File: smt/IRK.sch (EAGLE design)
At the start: 40 parts, among them IC1 PIC18F25K50, Q1 MMBT2222A, Q2 2N7002, Q3 2N7002, Q4 TSOP4838, Q5 MMBT3906

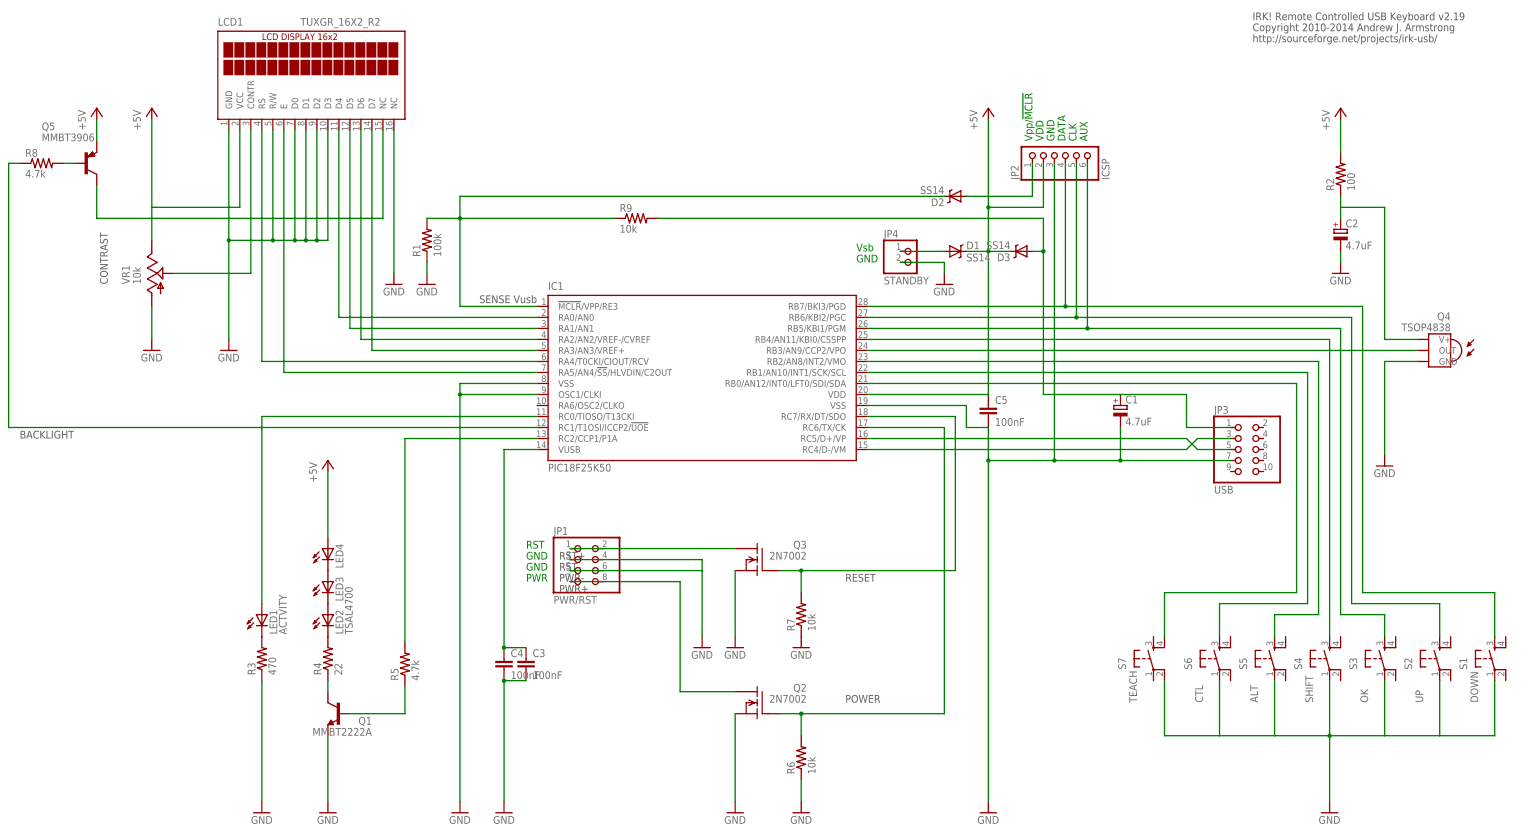
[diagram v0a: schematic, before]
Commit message: Reworked project structure to accommodate SMD and THT versions.
The orginal Through Hole Technology (THT) version is now stored
in the tht/ directory and the new Surface Mount Technology (SMT)
version is stored in the smt/ directory.
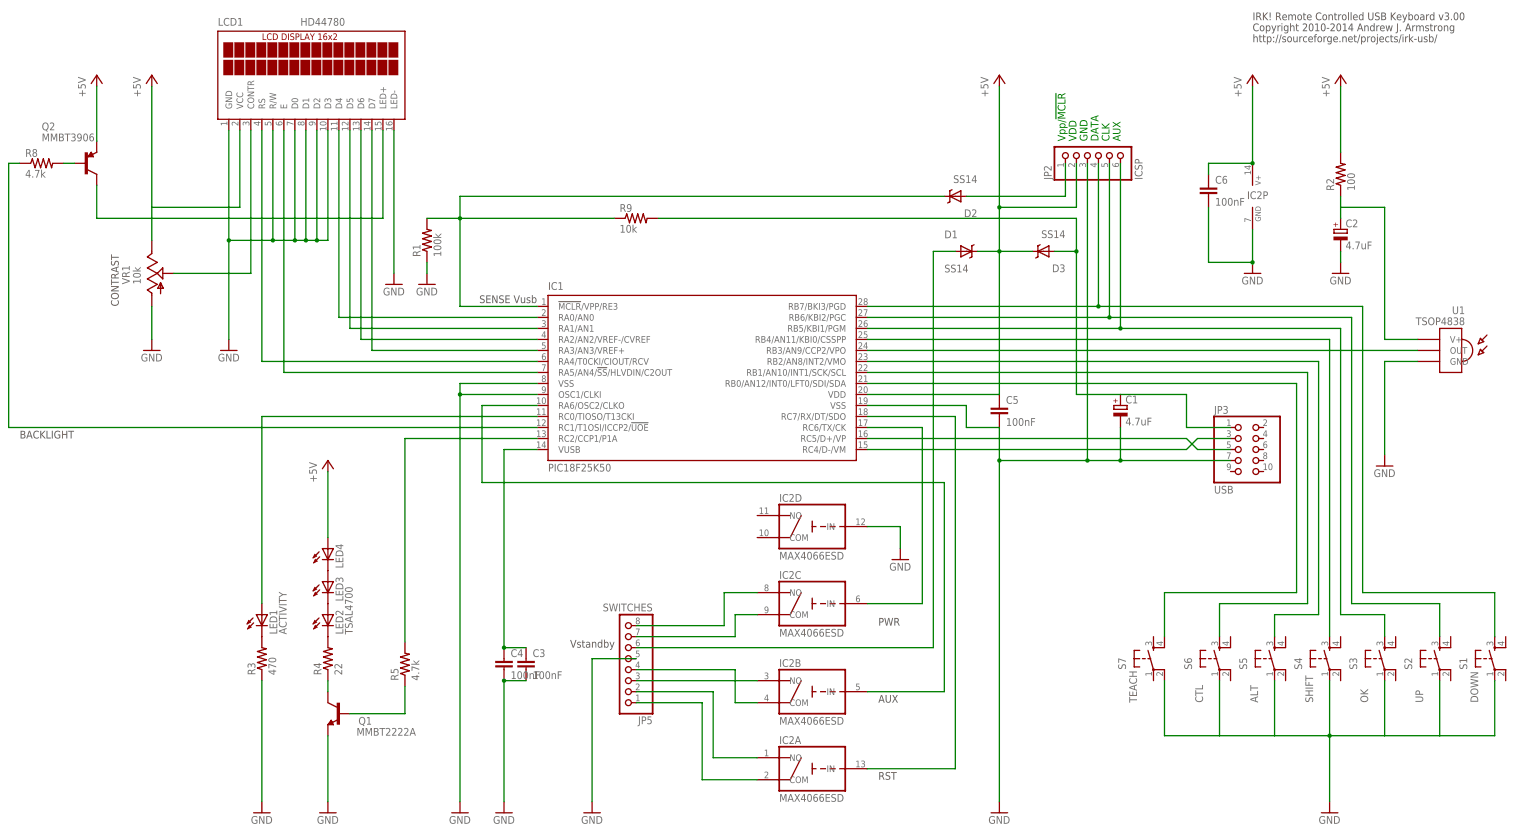
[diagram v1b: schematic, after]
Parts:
- removed JP1: PWR/RST, pinhead:PINHD-2X4
- removed JP4: STANDBY, pinhead:PINHD-1X2
- removed Q3: 2N7002, transistors_gaui:2N7002
- removed Q4: TSOP4838, tsop:TSOP4838
- removed Q5: MMBT3906, transistor-pnp:MMBT3906LT1SMD
- removed R6, R7: 10k, rcl:R-US_M1206
- added C6: 100nF, rcl:C-EUC0805
- added IC2: MAX4066ESD, irk:MAX4066ESD
- added JP5: SWITCHES, pinhead:PINHD-1X8
- added U1: TSOP4838, irk:TSOP4838
- D1, D2, D3: device SparkFun-DiscreteSemi:DIODE-SCHOTTKY_ -> irk:SS14
- LCD1: value TUXGR_16X2_R2 -> HD44780; device offboard:TUXGR_16X2_R2 -> irk:HD44780
- LED1: value ACTVITY -> ACTIVITY
- LED3, LED4: value (none) -> (none)
- Q1: device transistor:BC846A-NPN-SOT23-BEC -> irk:MMBT2222A
- Q2: value 2N7002 -> MMBT3906; device transistors_gaui:2N7002 -> irk:MMBT3906SOT23
- S1, S2, S3, S4, S5, S6, S7: device SparkFun-Electromechanical:TAC_SWITCHSMD -> irk:TAC_SWITCHPTH525
- VR1: device pot:TRIM_US-3223W -> irk:TRIMPOT3303W
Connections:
- removed net N$32: D1.A, JP4.1
- removed net N$37: IC1.RC6/TX/CK, Q2.G, R6.2
- removed net N$9: IC1.RC7/RX/DT/SDO, Q3.G, R7.2
- new net AUX: IC1.RA6/OSC2/CLKO, IC2B.IN
- new net N$33: IC2B.COM, JP5.4
- new net N$35: IC2B.NO, JP5.3
- new net N$39: IC2C.COM, JP5.7
- new net N$40: IC2C.NO, JP5.8
- new net PWR: IC1.RC6/TX/CK, IC2C.IN
- new net RST: IC1.RC7/RX/DT/SDO, IC2A.IN
- new net VSB: D1.A, JP5.6
- net +5V: now also C6.1, D1.K, D3.K, IC2P.V+, Q2.E; no longer D1.C, D3.C, Q5.E
- net GND: now also C6.2, IC2D.IN, IC2P.GND, JP5.5, LCD1.LED-, U1.GND; no longer JP1.3, JP1.4, JP1.5, JP1.6, JP4.2, LCD1.NC@2, Q2.S, Q3.S, Q4.GND, R6.1, R7.1
- net N$10: now also U1.OUT; no longer Q4.OUT
- net N$11: now also IC2A.COM, JP5.1; no longer JP1.1, JP1.2, Q3.D
- net N$22: now also IC2A.NO, JP5.2; no longer JP1.7, JP1.8, Q2.D
- net N$31: now also LCD1.LED+, Q2.C; no longer LCD1.NC@1, Q5.C
- net N$36: now also Q2.B; no longer Q5.B
- net N$50: now also U1.V+; no longer Q4.V+
- net N$8: now also D2.K; no longer D2.C
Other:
- note added: "IRK! Remote Controlled USB Keyboard v3.00"
- note added: "Vstandby"
- note removed: "IRK! Remote Controlled USB Keyboard v2.19"
- note removed: "POWER"
- note removed: "PWR+"
- note removed: "PWR-"
- note removed: "RESET"
- note removed: "RST+"
- note removed: "RST-"
- note removed: "Vsb"
- moved on the sheet: C5, JP2

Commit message: Changed symbol for push button switches
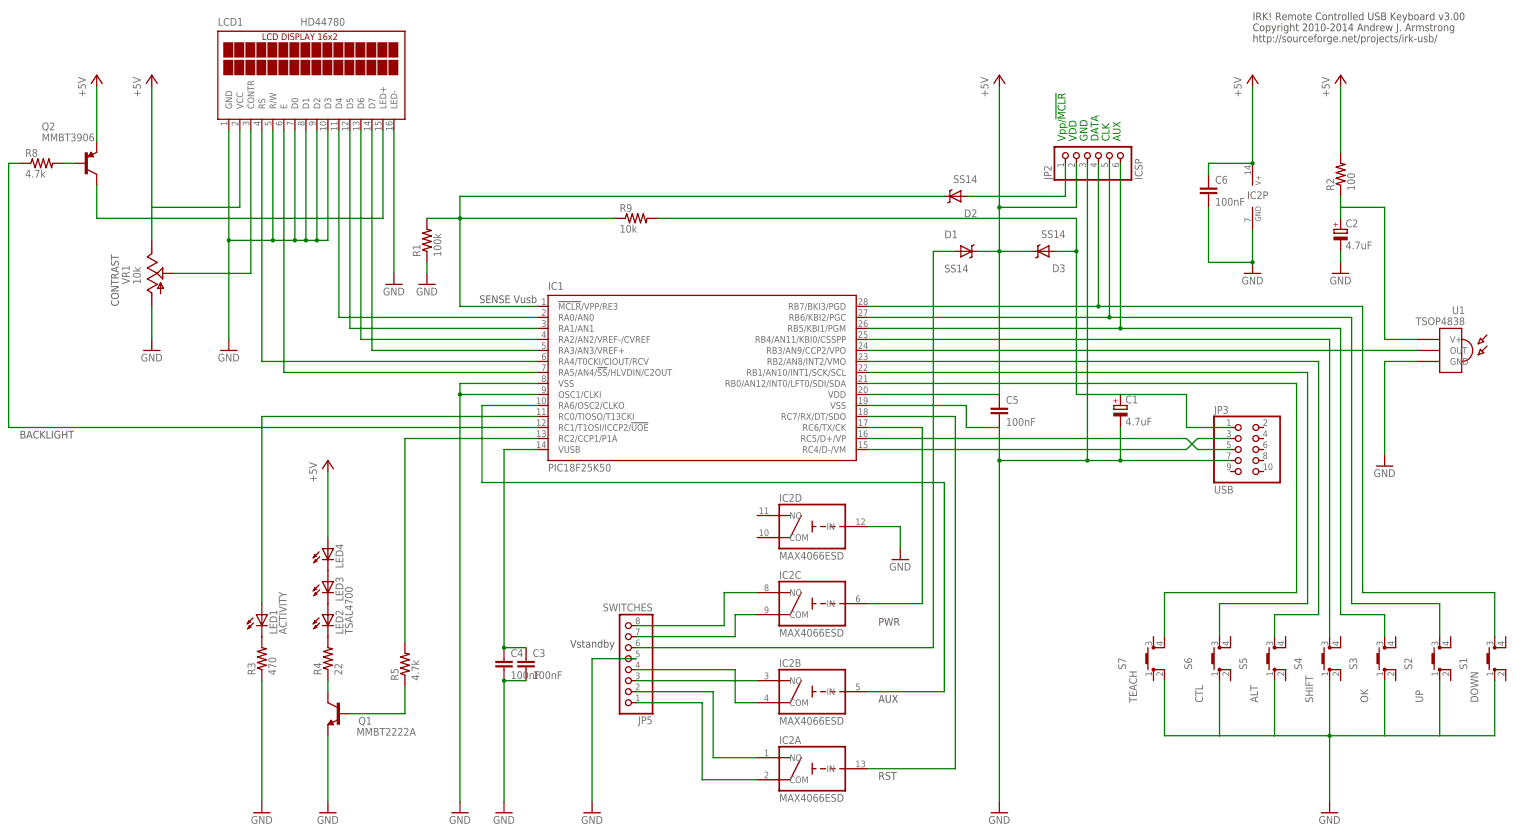
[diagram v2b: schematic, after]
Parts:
- S1, S2, S3, S4, S5, S6, S7: device irk:TAC_SWITCHPTH525 -> irk:C&K-PTS525-SM10
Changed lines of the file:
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@@
 <part name="C3" library="rcl" deviceset="C-EU" device="C0805" value="100nF"/>
 <part name="Q2" library="irk" deviceset="MMBT3906" device="SOT23" value="MMBT3906"/>
-<part name="S1" library="irk" deviceset="TAC_SWITCH" device="PTH525" value="DOWN"/>
-<part name="S2" library="irk" deviceset="TAC_SWITCH" device="PTH525" value="UP"/>
-<part name="S3" library="irk" deviceset="TAC_SWITCH" device="PTH525" value="OK"/>
-<part name="S4" library="irk" deviceset="TAC_SWITCH" device="PTH525" value="SHIFT"/>
-<part name="S5" library="irk" deviceset="TAC_SWITCH" device="PTH525" value="ALT"/>
-<part name="S6" library="irk" deviceset="TAC_SWITCH" device="PTH525" value="CTL"/>
-<part name="S7" library="irk" deviceset="TAC_SWITCH" device="PTH525" value="TEACH"/>
+<part name="S1" library="irk" deviceset="C&amp;K-PTS525" device="-SM10" value="DOWN"/>
+<part name="S2" library="irk" deviceset="C&amp;K-PTS525" device="-SM10" value="UP"/>
+<part name="S3" library="irk" deviceset="C&amp;K-PTS525" device="-SM10" value="OK"/>
+<part name="S4" library="irk" deviceset="C&amp;K-PTS525" device="-SM10" value="SHIFT"/>
+<part name="S5" library="irk" deviceset="C&amp;K-PTS525" device="-SM10" value="ALT"/>
+<part name="S6" library="irk" deviceset="C&amp;K-PTS525" device="-SM10" value="CTL"/>
+<part name="S7" library="irk" deviceset="C&amp;K-PTS525" device="-SM10" value="TEACH"/>
 <part name="D2" library="irk" deviceset="SS14" device="" value="SS14"/>
 <part name="D1" library="irk" deviceset="SS14" device="" value="SS14"/>
@@
 <instance part="C3" gate="G$1" x="38.1" y="-17.78"/>
 <instance part="Q2" gate="&gt;NAME" x="-63.5" y="96.52"/>
-<instance part="S1" gate="S" x="261.62" y="-17.78" smashed="yes" rot="R90">
+<instance part="S1" gate="&gt;NAME" x="261.62" y="-17.78" smashed="yes" rot="R90">
 <attribute name="NAME" x="255.27" y="-20.32" size="1.778" layer="95" rot="R90"/>
 <attribute name="VALUE" x="257.81" y="-27.94" size="1.778" layer="96" rot="R90"/>
 </instance>
-<instance part="S2" gate="S" x="248.92" y="-17.78" smashed="yes" rot="R90">
+<instance part="S2" gate="&gt;NAME" x="248.92" y="-17.78" smashed="yes" rot="R90">
 <attribute name="NAME" x="242.57" y="-20.32" size="1.778" layer="95" rot="R90"/>
 <attribute name="VALUE" x="245.11" y="-27.94" size="1.778" layer="96" rot="R90"/>
 </instance>
-<instance part="S3" gate="S" x="236.22" y="-17.78" smashed="yes" rot="R90">
+<instance part="S3" gate="&gt;NAME" x="236.22" y="-17.78" smashed="yes" rot="R90">
 <attribute name="NAME" x="229.87" y="-20.32" size="1.778" layer="95" rot="R90"/>
 <attribute name="VALUE" x="232.41" y="-27.94" size="1.778" layer="96" rot="R90"/>
 </instance>
-<instance part="S4" gate="S" x="223.52" y="-17.78" smashed="yes" rot="R90">
+<instance part="S4" gate="&gt;NAME" x="223.52" y="-17.78" smashed="yes" rot="R90">
 <attribute name="NAME" x="217.17" y="-20.32" size="1.778" layer="95" rot="R90"/>
 <attribute name="VALUE" x="219.71" y="-27.94" size="1.778" layer="96" rot="R90"/>
 </instance>
-<instance part="S5" gate="S" x="210.82" y="-17.78" smashed="yes" rot="R90">
+<instance part="S5" gate="&gt;NAME" x="210.82" y="-17.78" smashed="yes" rot="R90">
 <attribute name="NAME" x="204.47" y="-20.32" size="1.778" layer="95" rot="R90"/>
 <attribute name="VALUE" x="207.01" y="-27.94" size="1.778" layer="96" rot="R90"/>
 </instance>
-<instance part="S6" gate="S" x="198.12" y="-17.78" smashed="yes" rot="R90">
+<instance part="S6" gate="&gt;NAME" x="198.12" y="-17.78" smashed="yes" rot="R90">
 <attribute name="NAME" x="191.77" y="-20.32" size="1.778" layer="95" rot="R90"/>
 <attribute name="VALUE" x="194.31" y="-27.94" size="1.778" layer="96" rot="R90"/>
 </instance>
-<instance part="S7" gate="S" x="182.88" y="-17.78" smashed="yes" rot="R90">
+<instance part="S7" gate="&gt;NAME" x="182.88" y="-17.78" smashed="yes" rot="R90">
 <attribute name="NAME" x="176.53" y="-20.32" size="1.778" layer="95" rot="R90"/>
 <attribute name="VALUE" x="179.07" y="-27.94" size="1.778" layer="96" rot="R90"/>
@@
 <pinref part="IC1" gate="G$1" pin="RB7/BKI3/PGD"/>
 <pinref part="JP2" gate="A" pin="4"/>
-<pinref part="S1" gate="S" pin="3"/>
+<pinref part="S1" gate="&gt;NAME" pin="3"/>
 </segment>
 </net>
@@
 <pinref part="IC1" gate="G$1" pin="RB6/KBI2/PGC"/>
 <pinref part="JP2" gate="A" pin="5"/>
-<pinref part="S2" gate="S" pin="3"/>
+<pinref part="S2" gate="&gt;NAME" pin="3"/>
 </segment>
 </net>
@@
 <pinref part="IC1" gate="G$1" pin="RB5/KBI1/PGM"/>
 <pinref part="JP2" gate="A" pin="6"/>
-<pinref part="S3" gate="S" pin="3"/>
+<pinref part="S3" gate="&gt;NAME" pin="3"/>
 </segment>
 </net>
@@
 <wire x1="223.52" y1="55.88" x2="116.84" y2="55.88" width="0.1524" layer="91"/>
 <pinref part="IC1" gate="G$1" pin="RB4/AN11/KBI0/CSSPP"/>
-<pinref part="S4" gate="S" pin="3"/>
+<pinref part="S4" gate="&gt;NAME" pin="3"/>
 </segment>
 </net>
@@
 <wire x1="220.98" y1="50.8" x2="116.84" y2="50.8" width="0.1524" layer="91"/>
 <pinref part="IC1" gate="G$1" pin="RB2/AN8/INT2/VMO"/>
-<pinref part="S5" gate="S" pin="3"/>
+<pinref part="S5" gate="&gt;NAME" pin="3"/>
 </segment>
 </net>
@@
 <wire x1="218.44" y1="-5.08" x2="218.44" y2="48.26" width="0.1524" layer="91"/>
 <pinref part="IC1" gate="G$1" pin="RB1/AN10/INT1/SCK/SCL"/>
-<pinref part="S6" gate="S" pin="3"/>
+<pinref part="S6" gate="&gt;NAME" pin="3"/>
 </segment>
 </net>
@@
 <wire x1="215.9" y1="45.72" x2="116.84" y2="45.72" width="0.1524" layer="91"/>
 <pinref part="IC1" gate="G$1" pin="RB0/AN12/INT0/LFT0/SDI/SDA"/>
-<pinref part="S7" gate="S" pin="4"/>
+<pinref part="S7" gate="&gt;NAME" pin="4"/>
 </segment>
 </net>
@@
 <junction x="223.52" y="-35.56"/>
 <pinref part="GND29" gate="1" pin="GND"/>
-<pinref part="S1" gate="S" pin="1"/>
-<pinref part="S2" gate="S" pin="1"/>
-<pinref part="S3" gate="S" pin="1"/>
-<pinref part="S4" gate="S" pin="1"/>
-<pinref part="S5" gate="S" pin="1"/>
-<pinref part="S6" gate="S" pin="1"/>
-<pinref part="S7" gate="S" pin="2"/>
-</segment>
-<segment>
+<pinref part="S1" gate="&gt;NAME" pin="1"/>
+<pinref part="S2" gate="&gt;NAME" pin="1"/>
+<pinref part="S3" gate="&gt;NAME" pin="1"/>
+<pinref part="S4" gate="&gt;NAME" pin="1"/>
+<pinref part="S5" gate="&gt;NAME" pin="1"/>
+<pinref part="S6" gate="&gt;NAME" pin="1"/>
+<pinref part="S7" gate="&gt;NAME" pin="2"/>
+</segment>
+<segment>

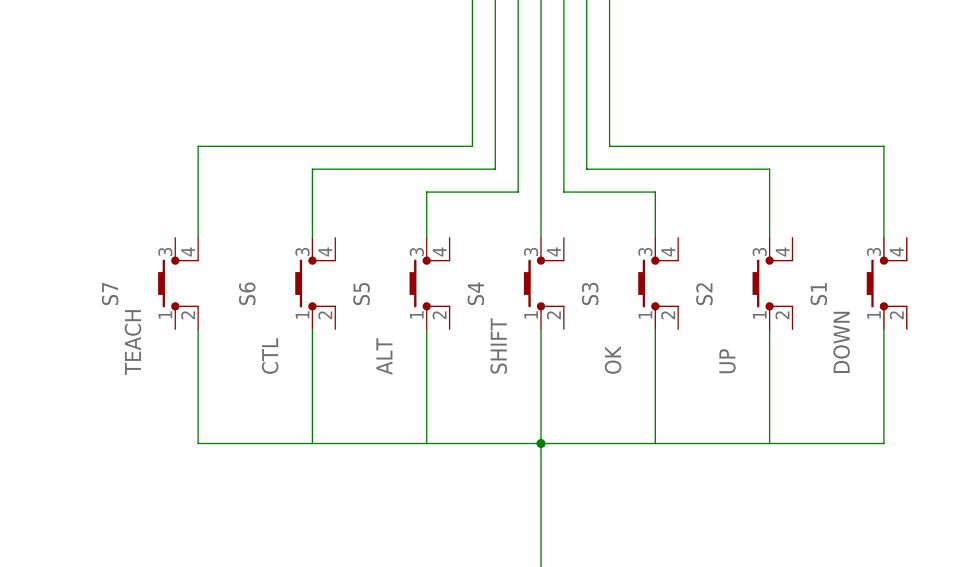
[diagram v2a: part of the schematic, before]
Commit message: Made cosmetic changes.
1. Used the HID Report Descriptor Decoder (http://sourceforge.net/projects/hidrdd/)
   to document the report descriptor meaning.
2. Changed the trimpot in IRK.lbr so that it has a tRestrict under it (this
   prevents copper traces being routed under the metal part of the trimpot).
3. Improved the routing of the track for the 100nF capacitor under the PIC18F25K50
   chip.
4. For the LCD library initialisation, used LAT registers instead of PORT registers
   (this probably doesn't make any difference to the operation).
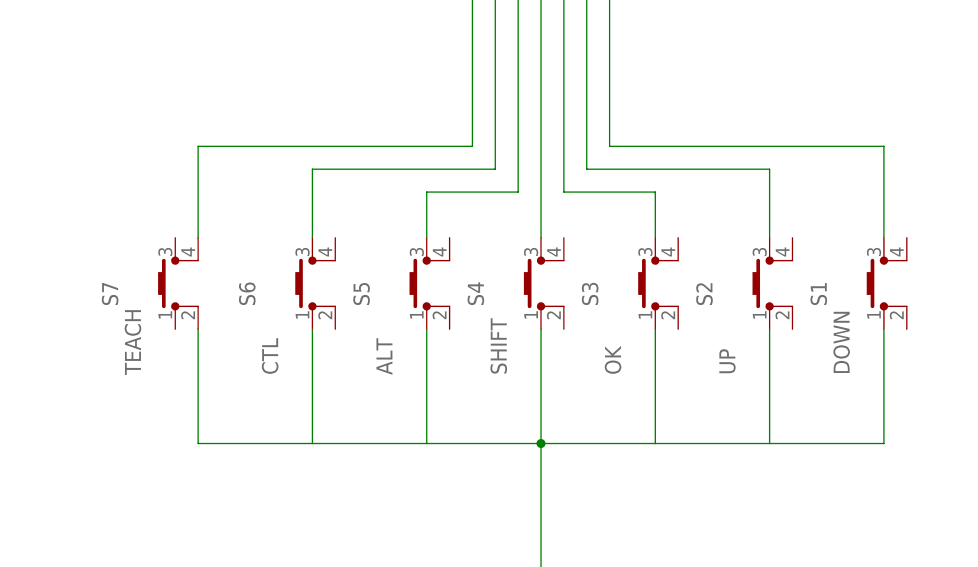
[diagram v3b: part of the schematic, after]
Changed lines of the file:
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@@
 <text x="119.38" y="-27.94" size="1.778" layer="97">AUX</text>
 <text x="48.26" y="-15.24" size="1.778" layer="97">Vstandby</text>
+<text x="205.74" y="121.92" size="1.778" layer="97">&gt;LAST_DATE_TIME</text>
 </plain>
 <instances>
